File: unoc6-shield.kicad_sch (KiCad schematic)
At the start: 6 parts, among them J1 DIN41612_02x05_AB_EvenPins, J2 DIN41612_02x05_AB_EvenPins, J3 DIN41612_02x05_AB_EvenPins, J4 DIN41612_02x05_AB_EvenPins, J5 DIN41612_02x05_AB_EvenPins, J6 DIN41612_02x05_AB_EvenPins

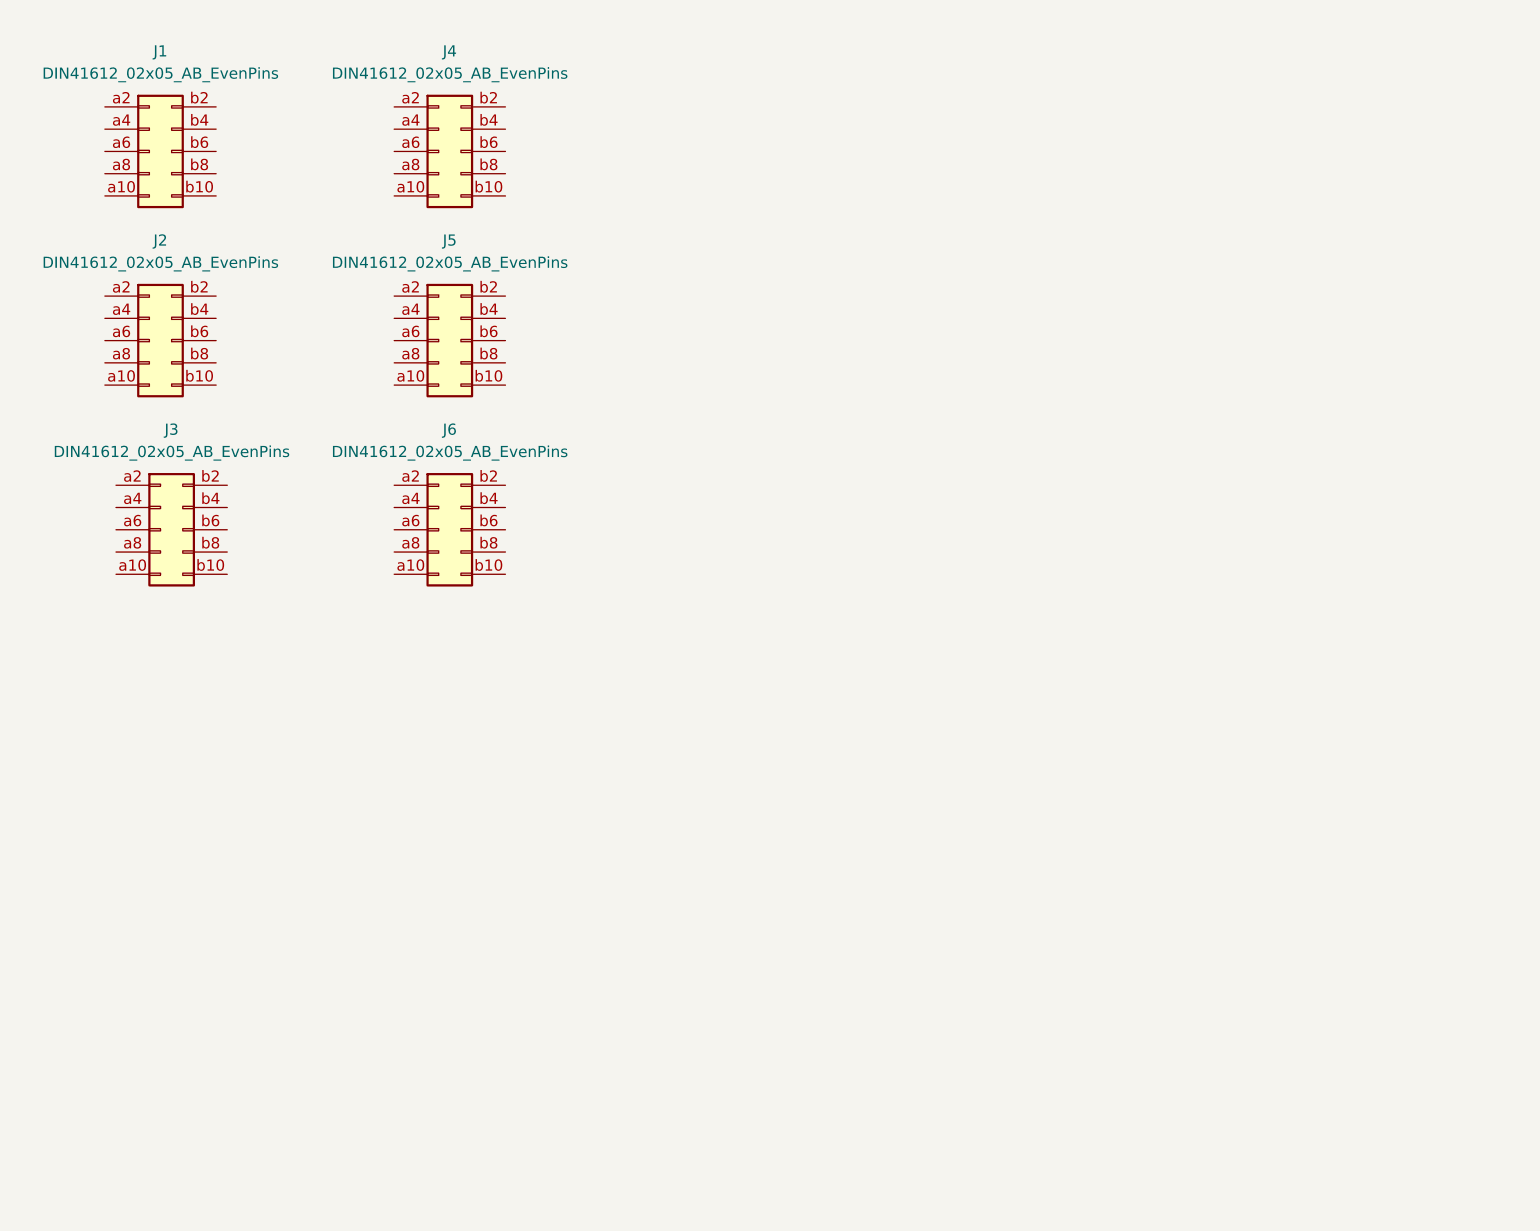
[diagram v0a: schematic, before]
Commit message: ax22 pin assignment & layout restructure
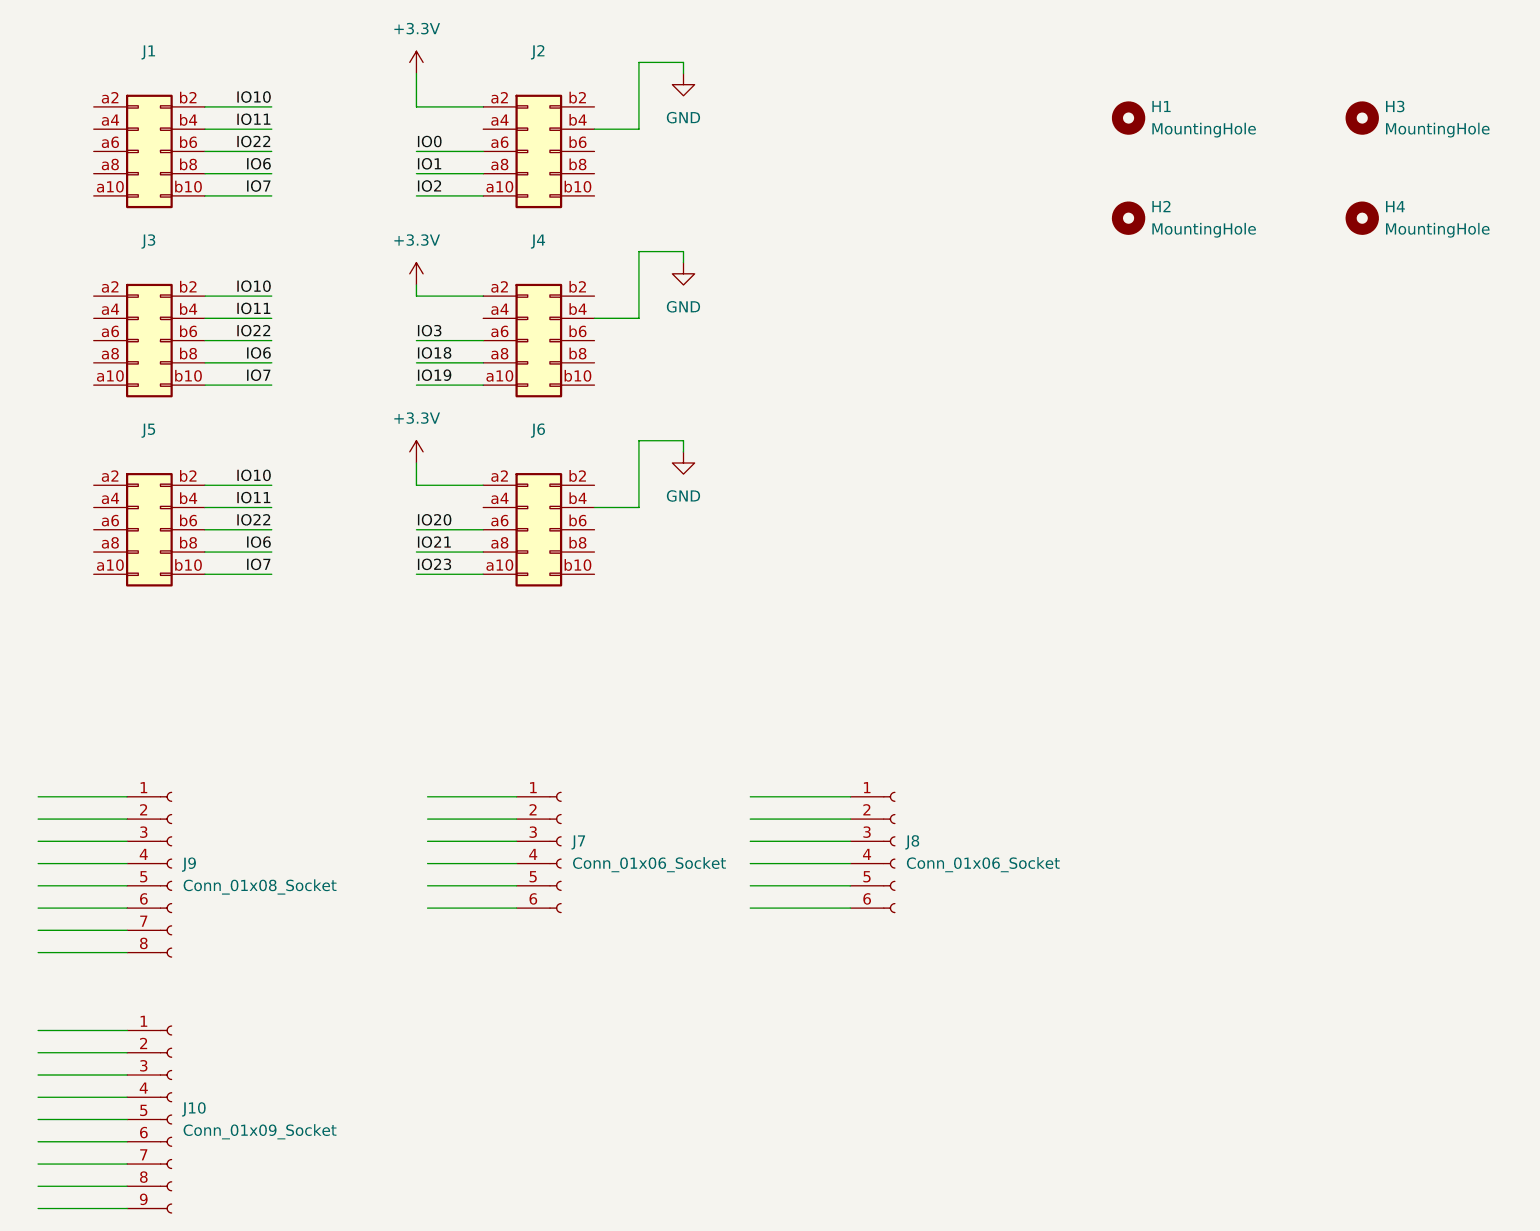
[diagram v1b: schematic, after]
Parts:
- removed J5: DIN41612_02x05_AB_EvenPins, symbol Connector:DIN41612_02x05_AB_EvenPins
- added H1, H2, H3, H4: MountingHole, MountingHole:MountingHole_2.1mm, symbol Mechanical:MountingHole
- added J10: Conn_01x09_Socket, Connector_PinSocket_2.00mm:PinSocket_1x09_P2.00mm_Vertical, symbol Connector:Conn_01x09_Socket
- added J2: DIN41612_02x05_AB_EvenPins, Connector_PinSocket_2.54mm:PinSocket_2x05_P2.54mm_Vertical_SMD, symbol Connector:DIN41612_02x05_AB_EvenPins
- added J7, J8: Conn_01x06_Socket, Connector_PinSocket_2.00mm:PinSocket_1x06_P2.00mm_Vertical, symbol Connector:Conn_01x06_Socket
- added J9: Conn_01x08_Socket, Connector_PinSocket_2.00mm:PinSocket_1x08_P2.00mm_Vertical, symbol Connector:Conn_01x08_Socket
- J1, J4, J6: footprint (none) -> Connector_PinSocket_2.54mm:PinSocket_2x05_P2.54mm_Vertical_SMD; KiLib_Generator (none) -> connector/pin_header_socket
- J3: renamed from J2; footprint (none) -> Connector_PinSocket_2.54mm:PinSocket_2x05_P2.54mm_Vertical_SMD; KiLib_Generator (none) -> connector/pin_header_socket
- J5: renamed from J3; footprint (none) -> Connector_PinSocket_2.54mm:PinSocket_2x05_P2.54mm_Vertical_SMD; KiLib_Generator (none) -> connector/pin_header_socket
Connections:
- net IO19: now reaches J4.a10 (Pin_a10)
- net +3.3V: now reaches J4.a2 (Pin_a2)
- net +3.3V: now also J6.a2 (Pin_a2), J2.a2 (Pin_a2)
- net IO3: now reaches J4.a6 (Pin_a6)
- net IO18: now reaches J4.a8 (Pin_a8)
- net GND: now reaches J4.b4 (Pin_b4)
- net GND: now also J6.b4 (Pin_b4), J2.b4 (Pin_b4)
- net IO7: now reaches J1.b10 (Pin_b10)
- net IO7: now also J3.b10 (Pin_b10), J5.b10 (Pin_b10)
- net IO10: now reaches J1.b2 (Pin_b2)
- net IO10: now also J3.b2 (Pin_b2), J5.b2 (Pin_b2)
- net IO11: now reaches J1.b4 (Pin_b4)
- net IO11: now also J3.b4 (Pin_b4), J5.b4 (Pin_b4)
- net IO22: now reaches J1.b6 (Pin_b6)
- net IO22: now also J3.b6 (Pin_b6), J5.b6 (Pin_b6)
- net IO6: now reaches J1.b8 (Pin_b8)
- net IO6: now also J3.b8 (Pin_b8), J5.b8 (Pin_b8)
- net IO23: now reaches J6.a10 (Pin_a10)
- net IO20: now reaches J6.a6 (Pin_a6)
- net IO21: now reaches J6.a8 (Pin_a8)
- new net IO0: J2.a6 (Pin_a6)
- new net IO1: J2.a8 (Pin_a8)
- new net IO2: J2.a10 (Pin_a10)
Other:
- moved on the sheet: J1, J3, J5
